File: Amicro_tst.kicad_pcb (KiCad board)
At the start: 2 copper layers, 16 parts, among them J1 Conn_01x04_Female, J2 Conn_01x05_Female, J3 Conn_01x04_Female, SW1 SW_Push, U1 ATmega328-P, U2 24LC512, Y1 Crystal

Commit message: 1
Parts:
- added (12): TP, TestPoint:TestPoint_THTPad_1.0x1.0mm_Drill0.5mm, F.Cu at (117.8, 117.4)
- added (13): TP, TestPoint:TestPoint_THTPad_1.0x1.0mm_Drill0.5mm, F.Cu at (115.2, 117.4)
- added (14): TP, TestPoint:TestPoint_THTPad_1.0x1.0mm_Drill0.5mm, F.Cu at (112.7, 117.4)
- added (24): TP, TestPoint:TestPoint_THTPad_1.0x1.0mm_Drill0.5mm, F.Cu at (135.6, 131.2)
- added (25): TP, TestPoint:TestPoint_THTPad_1.0x1.0mm_Drill0.5mm, F.Cu at (138.1, 131.2)
- added (26): TP, TestPoint:TestPoint_THTPad_1.0x1.0mm_Drill0.5mm, F.Cu at (140.4, 131.2)
- added (4): TP, TestPoint:TestPoint_THTPad_1.0x1.0mm_Drill0.5mm, F.Cu at (138.1, 117.3)
- added (5): TP, TestPoint:TestPoint_THTPad_1.0x1.0mm_Drill0.5mm, F.Cu at (135.8, 117.3)
- added (6): TP, TestPoint:TestPoint_THTPad_1.0x1.0mm_Drill0.5mm, F.Cu at (133.5, 117.3)
- added J4: Pow, TestPoint:TestPoint_2Pads_Pitch5.08mm_Drill1.3mm, F.Cu at (108.9, 126.9)
- added Q1: Q_NPN_BEC, Package_TO_SOT_SMD:SC-59_Handsoldering, B.Cu at (113.7, 136.1)
- added Q2: Q_NPN_BEC, Package_TO_SOT_SMD:SC-59_Handsoldering, B.Cu at (118.5, 136.1)
- added Q3: Q_NPN_BEC, Package_TO_SOT_SMD:SC-59_Handsoldering, B.Cu at (123.4, 136.1)
- added Q4: Q_NPN_BEC, Package_TO_SOT_SMD:SC-59_Handsoldering, B.Cu at (128.2, 136.1)
- added R10: 33, Resistor_SMD:R_0402_1005Metric, B.Cu at (110.2, 137.6)
- added R11: 33, Resistor_SMD:R_0402_1005Metric, B.Cu at (110.2, 138.6)
- added R12: 1k, Resistor_SMD:R_0402_1005Metric, F.Cu at (120.3, 130.5)
- added R5: 1k, Resistor_SMD:R_0402_1005Metric, F.Cu at (112.7, 130.5)
- added R6: 1k, Resistor_SMD:R_0402_1005Metric, F.Cu at (115.2, 130.5)
- added R7: 1k, Resistor_SMD:R_0402_1005Metric, F.Cu at (117.8, 130.5)
- added R8: 33, Resistor_SMD:R_0402_1005Metric, B.Cu at (110.2, 140.6)
- added R9: 33, Resistor_SMD:R_0402_1005Metric, B.Cu at (110.2, 139.6)
- C3: moved to B.Cu
- J1: value Conn_01x04_Female -> Sensor; footprint Connector_PinSocket_1.00mm:PinSocket_1x05_P1.00mm_Vertical -> Connector_JST:JST_EH_S4B-EH_1x04_P2.50mm_Horizontal
- J2: value Conn_01x05_Female -> Progmg
- J3: value Conn_01x04_Female -> Vibr; footprint Connector_JST:JST_EH_S4B-EH_1x04_P2.50mm_Horizontal -> Connector_PinSocket_1.00mm:PinSocket_1x04_P1.00mm_Vertical
- SW1: value SW_Push -> RESET
- moved J3 46.2 mm to (107.9, 137.6), turned to 0 degrees
- moved C3 26.7 mm to (129.2, 123.9)
- moved U2 23.2 mm to (157.6, 120.1)
- moved J1 19.7 mm to (142.9, 135.1), turned to 180 degrees
- moved J2 13.7 mm to (144.2, 113.7), turned to -90 degrees
- moved C4 9.68 mm to (127.7, 118.2), turned to 0 degrees
- moved C5 9.43 mm to (123.3, 118.2)
- moved R3 6.90 mm to (150.0, 130.4), turned to -90 degrees
- moved R4 6.78 mm to (152.6, 130.4), turned to -90 degrees
- moved R2 5.68 mm to (144.2, 123.4)
- moved SW1 5.43 mm to (145.5, 116.8)
- moved R1 2.54 mm to (125.4, 130.5)
- moved Y1 0.92 mm to (123.5, 114.7)
- moved C1 0.26 mm to (129.2, 130.2)
- moved D1 0.13 mm to (122.9, 131.2)
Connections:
- J1 pad 4: /5V -> VCC
- J3 pad 1: unconnected-(J3-Pad1) -> Net-(R10-Pad2)
- J3 pad 2: unconnected-(J3-Pad2) -> Net-(R11-Pad2)
- J3 pad 3: unconnected-(J3-Pad3) -> Net-(R9-Pad2)
- J3 pad 4: unconnected-(J3-Pad4) -> Net-(R8-Pad2)
- U1 pad 12: unconnected-(U1-Pad12) -> Net-(TP3(12)1-Pad1)
- U1 pad 13: unconnected-(U1-Pad13) -> Net-(TP1(13)1-Pad1)
- U1 pad 14: unconnected-(U1-Pad14) -> Net-(TP2(14)1-Pad1)
- U1 pad 15: unconnected-(U1-Pad15) -> PWM0
- U1 pad 16: unconnected-(U1-Pad16) -> PWM1
- U1 pad 17: unconnected-(U1-Pad17) -> PWM2
- U1 pad 18: unconnected-(U1-Pad18) -> PWM3
- U1 pad 24: unconnected-(U1-Pad24) -> Net-(TP(24)1-Pad1)
- U1 pad 25: unconnected-(U1-Pad25) -> Net-(TP(25)1-Pad1)
- U1 pad 26: unconnected-(U1-Pad26) -> Net-(TP(26)1-Pad1)
- U1 pad 4: unconnected-(U1-Pad4) -> Net-(TP(4)1-Pad1)
- U1 pad 5: unconnected-(U1-Pad5) -> Net-(TP(7)1-Pad1)
- U1 pad 6: unconnected-(U1-Pad6) -> Net-(TP(6)1-Pad1)
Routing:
- net VCC: track 0.00 -> 2.03 mm
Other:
- board text added: "(+) (-)"

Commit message: Update Amicro_tst.kicad_pcb
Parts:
- J1: footprint Connector_JST:JST_EH_S4B-EH_1x04_P2.50mm_Horizontal -> Connector_JST:JST_EH_B4B-EH-A_1x04_P2.50mm_Vertical
- moved J3 4.01 mm to (106.1, 134.0)
- moved R11 4.01 mm to (108.4, 135.0)
- moved R9 4.01 mm to (108.4, 136.0)
- moved R10 4.01 mm to (108.4, 134.0)
- moved R8 4.01 mm to (108.4, 137.1)
- moved SW1 3.30 mm to (142.2, 116.8)
- moved J1 1.03 mm to (142.7, 136.1)

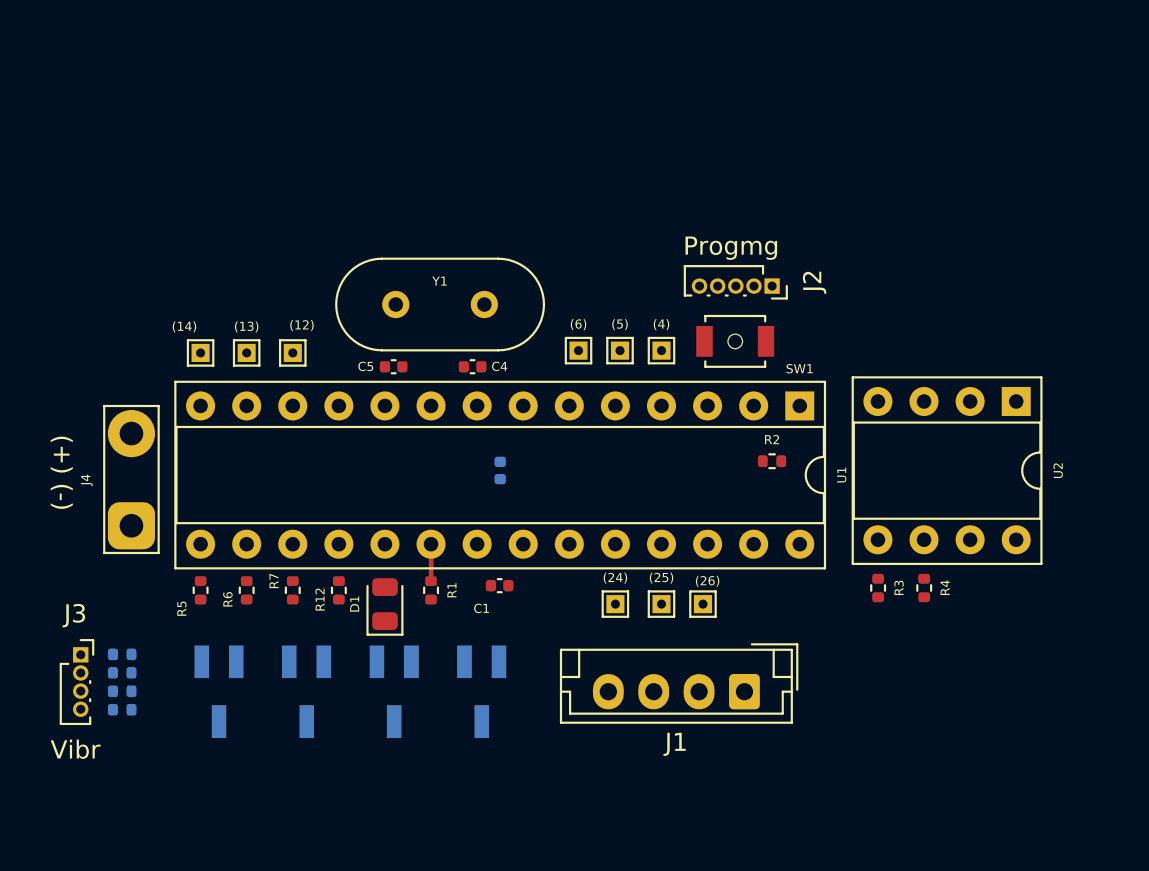
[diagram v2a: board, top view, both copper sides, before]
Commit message: Routing & Layout
did some routing and changed layout
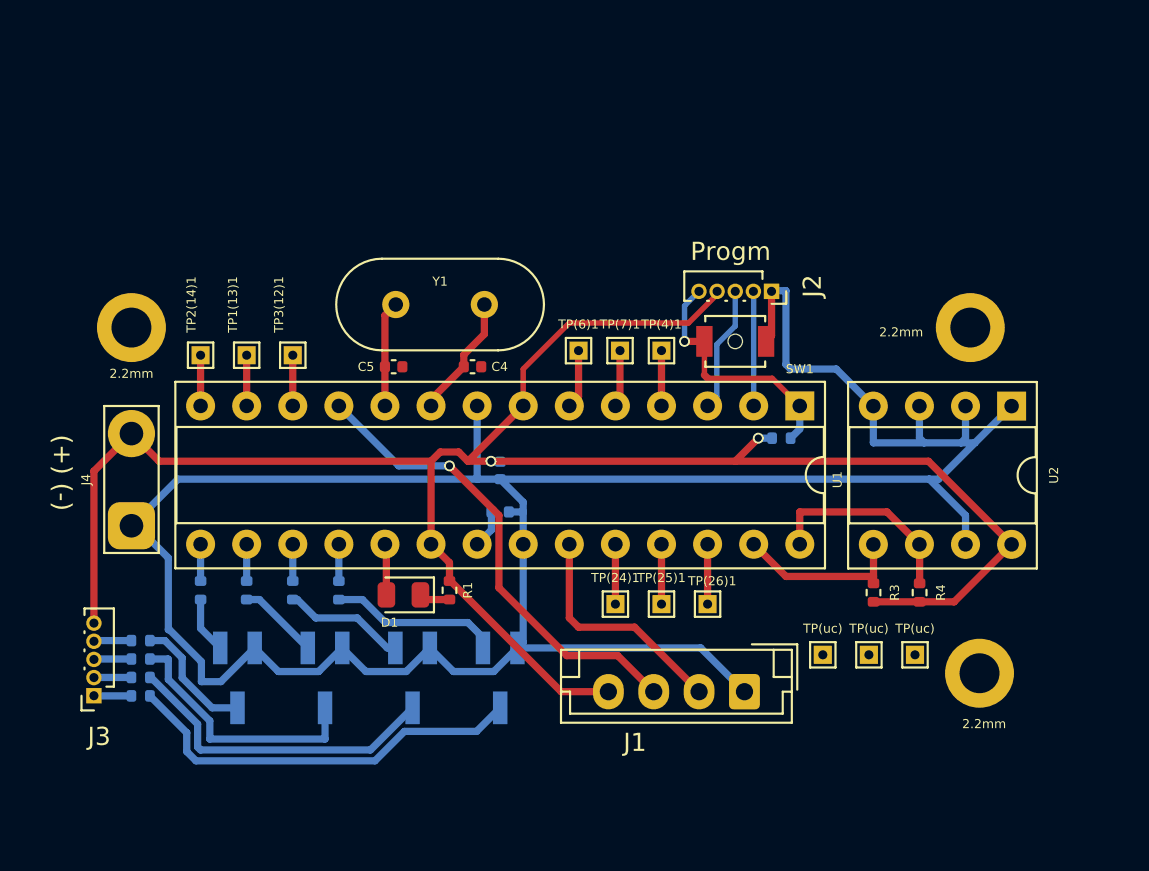
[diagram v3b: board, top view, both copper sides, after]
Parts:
- added 2.2mm: 2.2, MountingHole:MountingHole_2.2mm_M2_DIN965_Pad, F.Cu at (155.6, 135.1)
- added 2.2mm: 2.2, MountingHole:MountingHole_2.2mm_M2_DIN965_Pad, F.Cu at (155.1, 116.0)
- added 2.2mm: 2.2, MountingHole:MountingHole_2.2mm_M2_DIN965_Pad, F.Cu at (108.9, 116.0)
- added TP(uc): TP, TestPoint:TestPoint_THTPad_1.0x1.0mm_Drill0.5mm, F.Cu at (147.0, 134.0)
- added TP(uc): TP, TestPoint:TestPoint_THTPad_1.0x1.0mm_Drill0.5mm, F.Cu at (149.5, 134.0)
- added TP(uc): TP, TestPoint:TestPoint_THTPad_1.0x1.0mm_Drill0.5mm, F.Cu at (152.1, 134.0)
- C1, R12, R2, R5, R6, R7: moved to B.Cu
- J2: value Progmg -> Progm
- J3: footprint Connector_PinSocket_1.00mm:PinSocket_1x04_P1.00mm_Vertical -> Connector_PinSocket_1.00mm:PinSocket_1x05_P1.00mm_Vertical
- moved C1 4.06 mm to (129.2, 126.2)
- moved J3 2.37 mm to (106.8, 136.3), turned to 180 degrees
- moved R2 1.37 mm to (144.7, 122.1)
- moved Q4 1.27 mm to (129.2, 135.3)
- moved Q1 1.27 mm to (114.7, 135.3)
- moved Q2 1.27 mm to (119.6, 135.3)
- moved Q3 1.27 mm to (124.4, 135.3)
- moved R10 1.27 mm to (109.4, 133.3)
- moved R11 1.27 mm to (109.4, 134.3)
- moved R8 1.27 mm to (109.4, 136.3)
- moved R9 1.27 mm to (109.4, 135.3)
- moved D1 1.14 mm to (123.9, 130.7), turned to 180 degrees
- moved R1 1.02 mm to (126.4, 130.5)
- moved R3 0.36 mm to (149.8, 130.6)
- moved U2 0.36 mm to (157.4, 120.3)
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- renumbered (24) to TP(24)1, (25) to TP(25)1, (26) to TP(26)1, (4) to TP(4)1, (6) to TP(6)1, (5) to TP(7)1, (13) to TP1(13)1, (14) to TP2(14)1, (12) to TP3(12)1
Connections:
- J3 pad 1: Net-(R10-Pad2) -> Net-(R8-Pad2)
- J3 pad 2: Net-(R11-Pad2) -> Net-(R9-Pad2)
- J3 pad 3: Net-(R9-Pad2) -> Net-(R11-Pad2)
- J3 pad 4: Net-(R8-Pad2) -> Net-(R10-Pad2)
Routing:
- net GND: track 0.00 -> 141.1 mm
- net VCC: track 2.03 -> 112.0 mm, vias 0 -> 2
- net PW: track 0.00 -> 26.2 mm, vias 0 -> 1
- net Net-(Q4-Pad3): track 0.00 -> 22.6 mm
- net Net-(Q3-Pad3): track 0.00 -> 17.8 mm
- net Net-(Q2-Pad3): track 0.00 -> 14.4 mm
- net RESET: track 0.00 -> 14.0 mm, vias 0 -> 1
- net AN: track 0.00 -> 12.9 mm
- net SCL: track 0.00 -> 11.3 mm
- net SDA: track 0.00 -> 9.49 mm
- net Net-(Q4-Pad1): track 0.00 -> 9.38 mm
- net Net-(Q1-Pad3): track 0.00 -> 7.00 mm
- net TXD: track 0.00 -> 6.95 mm
- net Net-(C4-Pad1): track 0.00 -> 6.80 mm
- net Net-(Q3-Pad1): track 0.00 -> 6.76 mm
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
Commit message: Added ouline and lables
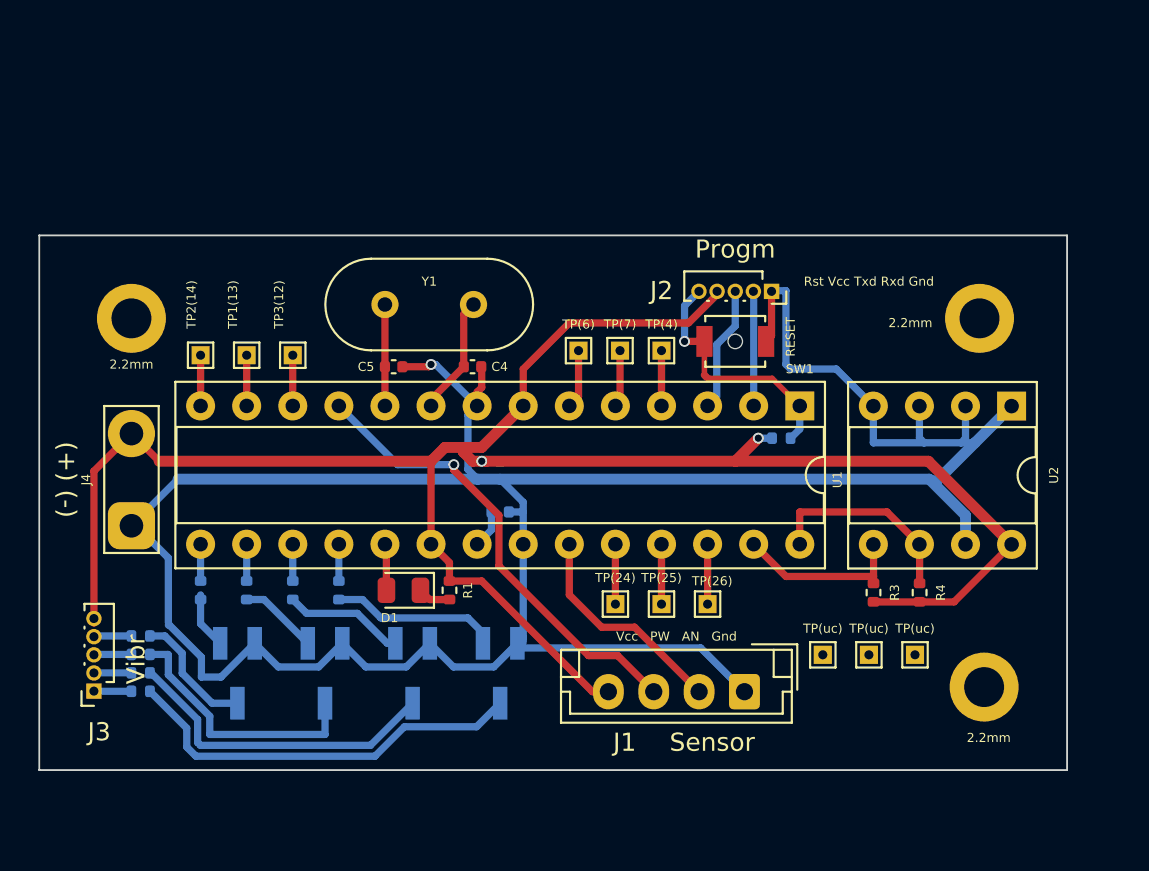
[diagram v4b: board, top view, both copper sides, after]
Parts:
- moved 2.2mm 0.80 mm to (155.9, 135.8)
- moved 2.2mm 0.72 mm to (155.6, 115.5)
- moved Y1 0.60 mm to (122.9, 114.7)
- moved 2.2mm 0.51 mm to (108.9, 115.5)
- moved D1 0.25 mm to (123.9, 130.5)
- moved Q1 0.25 mm to (114.7, 135.1)
- moved Q2 0.25 mm to (119.6, 135.1)
- moved Q3 0.25 mm to (124.4, 135.1)
- moved Q4 0.25 mm to (129.2, 135.1)
- moved R10 0.25 mm to (109.4, 133.0)
- moved R8 0.25 mm to (109.4, 136.0)
- moved J3 0.25 mm to (106.8, 136.0)
- moved R11 0.25 mm to (109.4, 134.0)
- moved R9 0.25 mm to (109.4, 135.0)
- renumbered TP(24)1 to TP(24), TP(25)1 to TP(25), TP(26)1 to TP(26), TP(4)1 to TP(4), TP(6)1 to TP(6), TP(7)1 to TP(7), TP1(13)1 to TP1(13), TP2(14)1 to TP2(14), TP3(12)1 to TP3(12)
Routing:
- net GND: track 141.1 -> 148.6 mm, vias 0 -> 1
- net AN: track 12.9 -> 12.2 mm
- net VCC: track 112.0 -> 112.5 mm
- net PW: track 26.2 -> 25.7 mm
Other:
- board outline added: 56.6 x 29.5 mm
- board text added: "Rst Vcc Txd Rxd Gnd"
- board text added: "Vcc PW AN Gnd"

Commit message: Hole Alignment And Added tstpnt
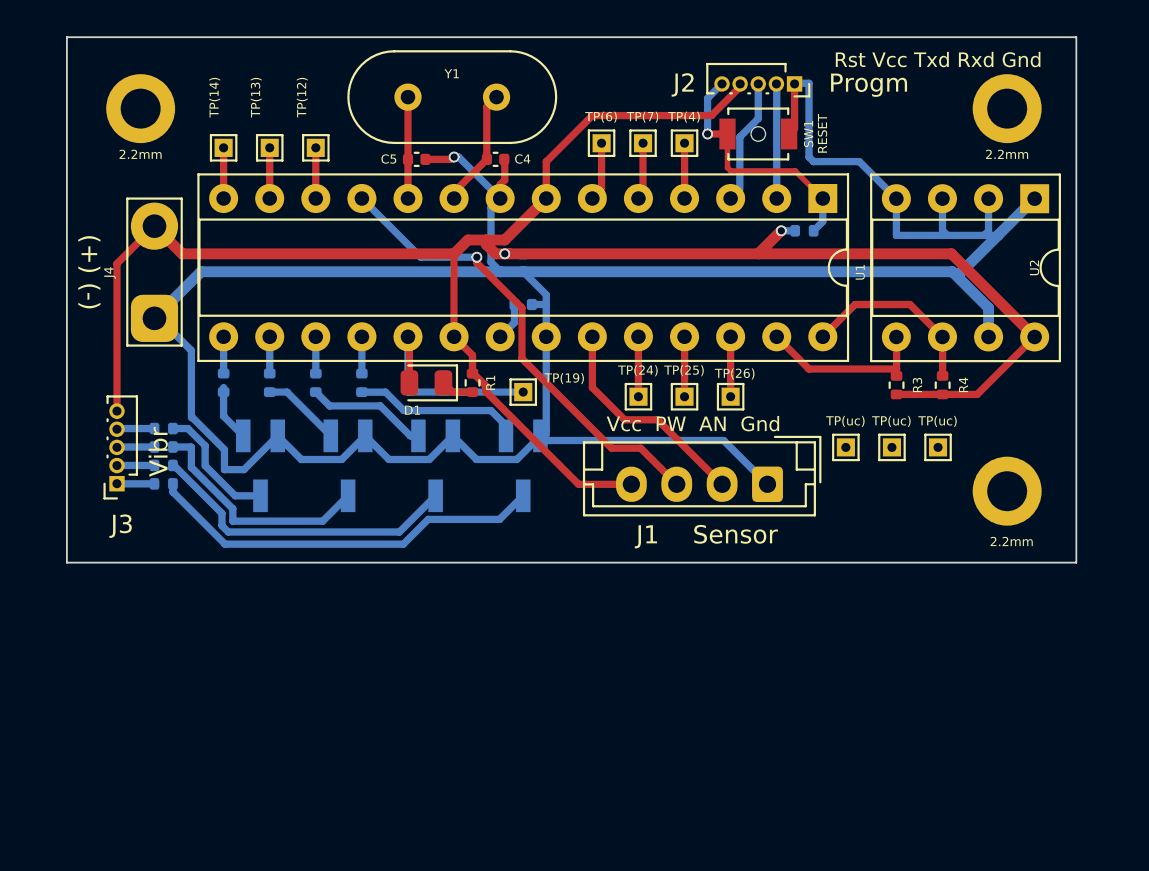
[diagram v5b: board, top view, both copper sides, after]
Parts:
- added TP(19): TP, TestPoint:TestPoint_THTPad_1.0x1.0mm_Drill0.5mm, F.Cu at (130.5, 119.6)
- R1: value R -> 50
- moved 2.2mm 11.7 mm to (157.2, 103.9)
- moved 2.2mm 11.6 mm to (109.4, 103.9)
- moved J1 11.5 mm to (143.9, 124.6)
- moved J2 11.5 mm to (145.4, 102.6)
- moved R11 11.5 mm to (110.7, 122.6)
- moved R6 11.5 mm to (116.5, 119.0)
- moved R9 11.5 mm to (110.7, 123.6)
- moved TP(4) 11.5 mm to (139.4, 105.8)
- moved TP(6) 11.5 mm to (134.8, 105.8)
- moved TP(7) 11.5 mm to (137.1, 105.8)
- moved TP(uc) 11.5 mm to (150.8, 122.6)
- moved TP(uc) 11.5 mm to (153.3, 122.6)
- moved C5 11.5 mm to (124.6, 106.7)
- moved J3 11.5 mm to (108.1, 124.6)
- moved J4 11.5 mm to (110.2, 115.5)
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- renumbered TP3(12) to TP(12), TP1(13) to TP(13), TP2(14) to TP(14)
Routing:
- net Net-(D1-Pad2): track 2.83 -> 12.2 mm
- net Net-(Q2-Pad3): track 14.4 -> 13.0 mm
- net SCL: track 11.3 -> 10.2 mm
- net Net-(Q3-Pad3): track 17.8 -> 17.2 mm
- net Net-(Q4-Pad3): track 22.6 -> 22.0 mm
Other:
- board size 56.6 x 29.5 mm -> 55.6 x 29 mm

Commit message: Motor schem Wrong, need redo
old gerber files available, messed up on motor schematic, fixed schematic, need to rewire and fix board
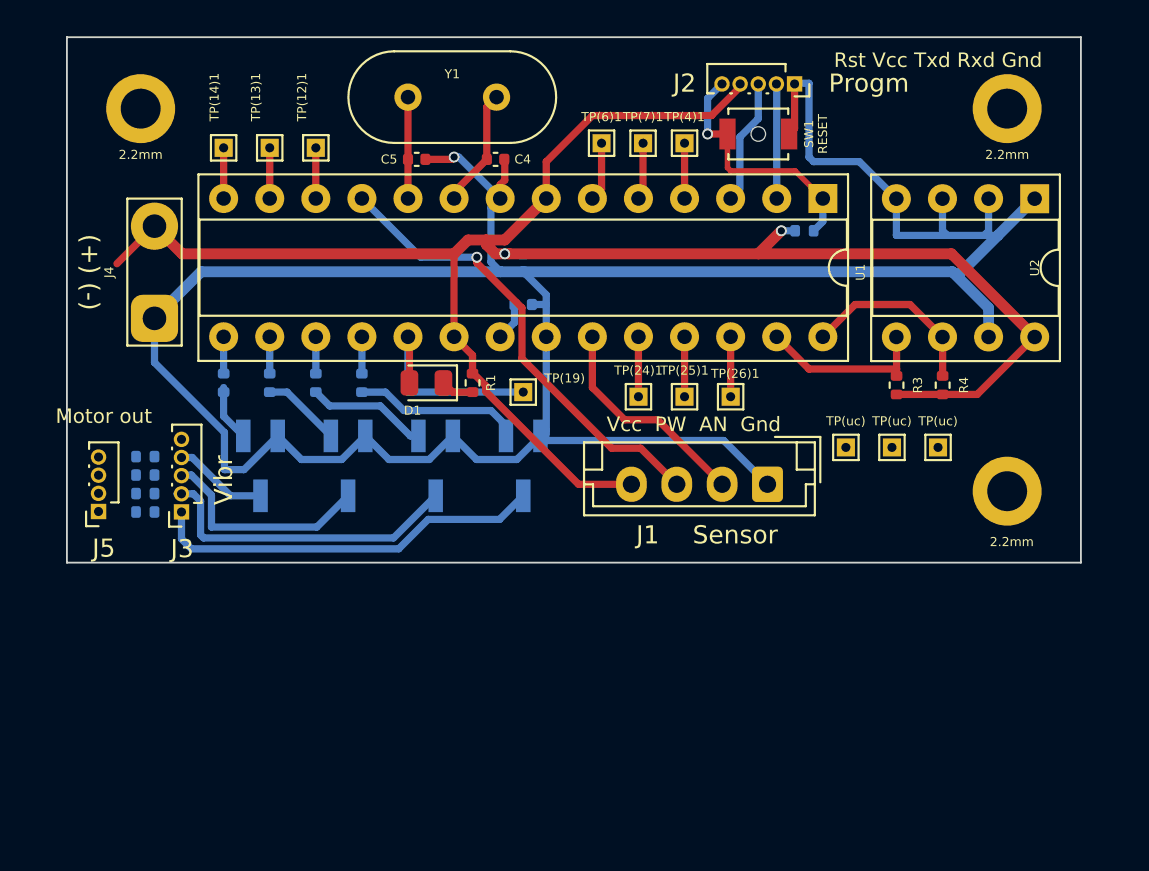
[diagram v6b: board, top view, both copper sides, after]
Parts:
- added J5: Motor out, Connector_PinSocket_1.00mm:PinSocket_1x04_P1.00mm_Vertical, F.Cu at (107.1, 126.1)
- moved J3 3.88 mm to (111.6, 126.2)
- moved R11 3.72 mm to (109.7, 126.2), turned to 0 degrees
- moved R10 3.72 mm to (109.7, 125.1), turned to 0 degrees
- moved R8 1.81 mm to (109.7, 123.1), turned to 0 degrees
- moved R9 1.15 mm to (109.7, 124.1), turned to 0 degrees
- renumbered TP(12) to TP(12)1, TP(13) to TP(13)1, TP(14) to TP(14)1, TP(24) to TP(24)1, TP(25) to TP(25)1, TP(26) to TP(26)1, TP(4) to TP(4)1, TP(6) to TP(6)1, TP(7) to TP(7)1
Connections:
- J3 pad 1: Net-(J3-Pad1) -> M3
- J3 pad 2: Net-(J3-Pad2) -> M2
- J3 pad 3: Net-(J3-Pad3) -> M1
- J3 pad 4: Net-(J3-Pad4) -> M0
- Q1 pad 3: Net-(Q1-Pad3) -> M0
- Q2 pad 3: Net-(Q2-Pad3) -> M1
- Q3 pad 3: Net-(Q3-Pad3) -> M2
- Q4 pad 3: Net-(Q4-Pad3) -> M3
- R10 pad 1: Net-(Q1-Pad3) -> Mt2+
- R10 pad 2: Net-(J3-Pad4) -> VCC
- R11 pad 1: Net-(Q2-Pad3) -> Mt3+
- R11 pad 2: Net-(J3-Pad3) -> VCC
- R8 pad 1: Net-(Q4-Pad3) -> Mt0+
- R8 pad 2: Net-(J3-Pad1) -> VCC
- R9 pad 1: Net-(Q3-Pad3) -> Mt1+
- R9 pad 2: Net-(J3-Pad2) -> VCC
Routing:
- net Net-(Q4-Pad3): track 22.0 -> 0.00 mm
- net M3: track 0.00 -> 21.8 mm
- net M2: track 0.00 -> 17.3 mm
- net Net-(Q3-Pad3): track 17.2 -> 0.00 mm
- net Net-(Q2-Pad3): track 13.0 -> 0.00 mm
- net M1: track 0.00 -> 12.1 mm
- net VCC: track 112.7 -> 104.3 mm
- net Net-(Q1-Pad3): track 7.00 -> 0.00 mm
- net M0: track 0.00 -> 5.23 mm
- net Net-(J3-Pad4): track 2.08 -> 0.00 mm
- net Net-(J3-Pad3): track 2.08 -> 0.00 mm
- net Net-(J3-Pad1): track 2.07 -> 0.00 mm
- net Net-(J3-Pad2): track 2.07 -> 0.00 mm
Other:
- board size 55.6 x 29 mm -> 55.9 x 29 mm
